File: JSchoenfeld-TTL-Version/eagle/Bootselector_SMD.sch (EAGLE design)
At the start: 13 parts, among them IC3 74HCT00D, IC4 74HCT157D

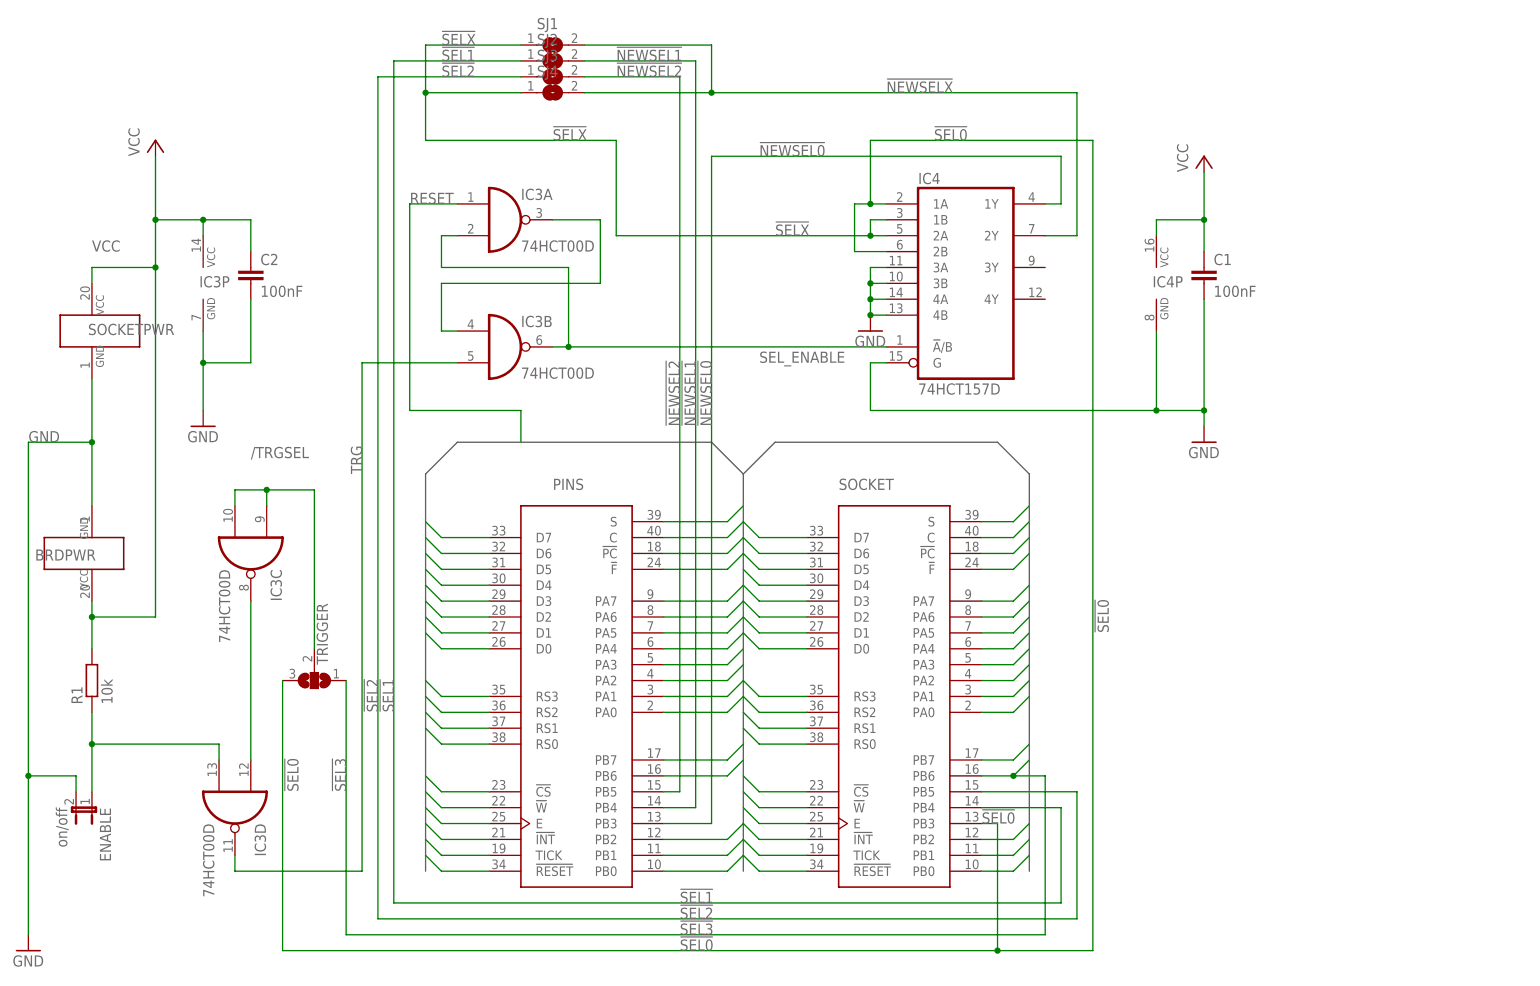
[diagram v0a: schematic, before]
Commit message: 25.02.2018 - Fredric QJ Blåholtz (e5frog) + Marko Oette (marko@oette.info) v. 0.98 - Prototyping v 0.97 done, works - Updated SMD version to match THT version - Updated documentation for THT version - Added mouse enable / disable documentation
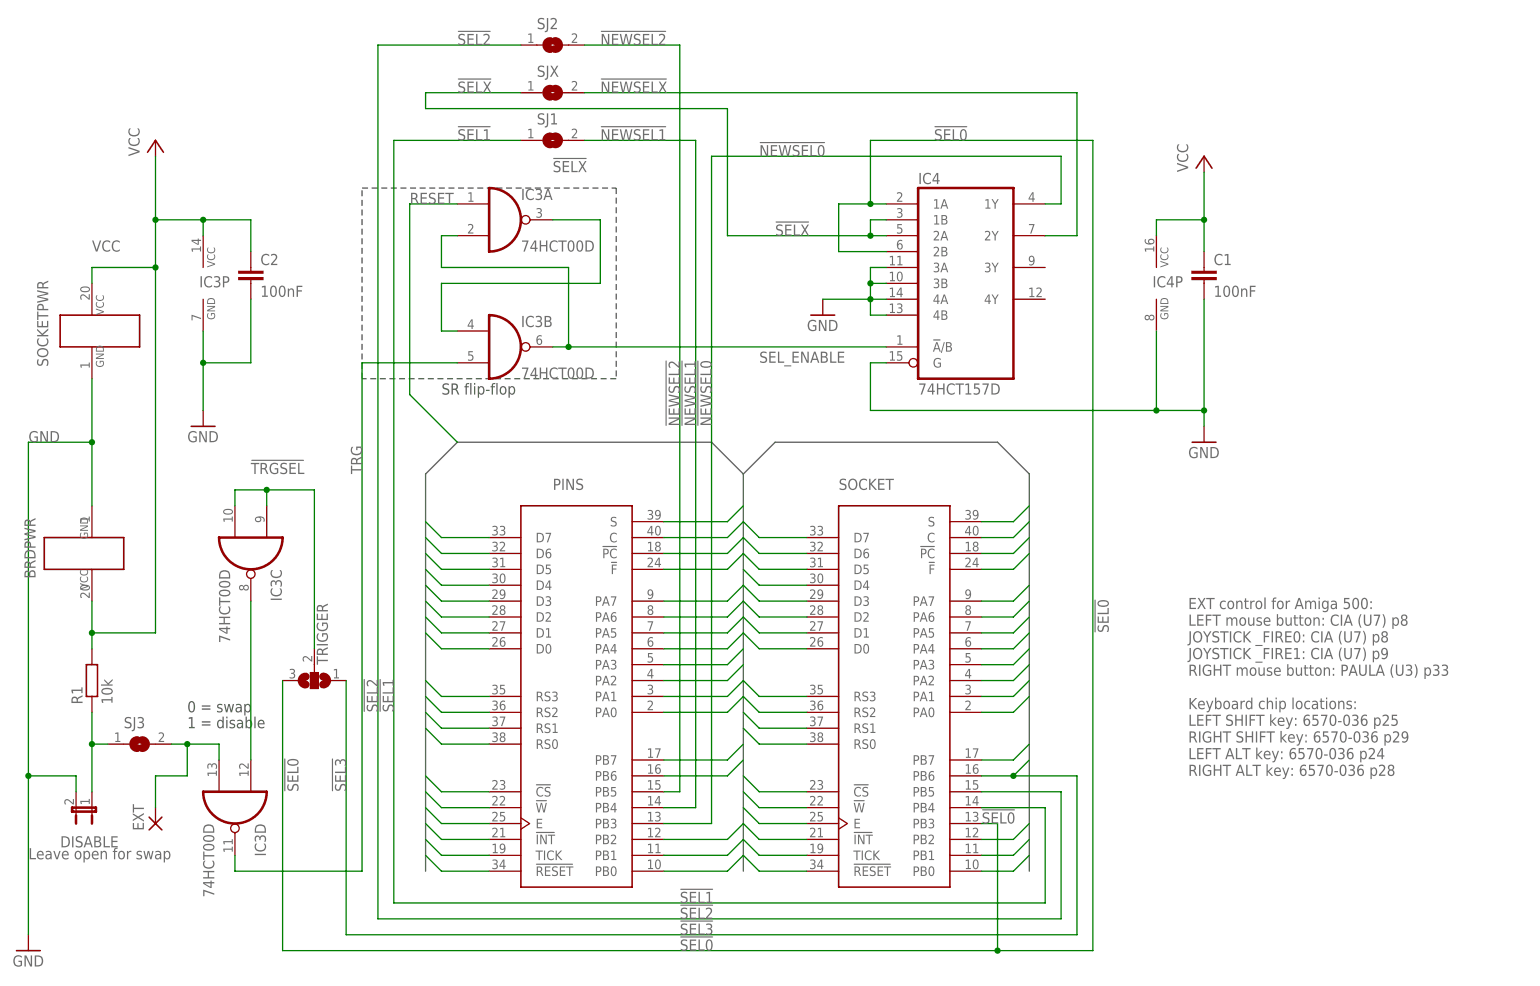
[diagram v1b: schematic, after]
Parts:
- added EXT: (no value), wirepad:SMD2
- DISABLE: value on/off -> Leave open for swap
- renumbered ENABLE to DISABLE, SJ4 to SJX
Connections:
- net /TRGSEL renamed !TRGSEL
- removed net N$2: DISABLE.1, IC3D.I1, R1.1
- new net N$1: EXT.P, IC3D.I1, SJ3.2
- new net N$23: DISABLE.1, R1.1, SJ3.1
- net !NEWSEL1: now also SJ1.2; no longer SJ2.2
- net !NEWSEL2: now also SJ2.2; no longer SJ3.2
- net !NEWSELX: no longer SJ1.2
- net !SEL1: now also SJ1.1; no longer SJ2.1
- net !SEL2: now also SJ2.1; no longer SJ3.1
- net !SELX: no longer SJ1.1
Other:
- note added: "0 = swap"
- note added: "1 = disable"
- note added: "EXT control for Amiga 500: LEFT mouse button: CIA (U7) p8 JOYSTICK _FIRE0: CIA (U7) p8 JOYSTICK _FIRE1: CIA (U7) p9 RIGHT mouse button: PAULA (U3) p33 Keyboard chip locations: LEFT SHIFT key: 6570-036 p25 RIGHT SHIFT key: 6570-036 p29 LEFT ALT key: 6570-036 p24 RIGHT ALT key: 6570-036 p28"
- note added: "SR flip-flop"
- moved on the sheet: SJ1, SJ2, SJ3
